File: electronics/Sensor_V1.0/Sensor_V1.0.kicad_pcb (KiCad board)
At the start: 2 copper layers, 45.9 x 25.6 mm, 7 parts, among them J1 nuclone_small_left, J2 nuclone_small_right, J3 PINS_1X18, J4 PINS_1X17

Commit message: WIP schematic definition
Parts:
- added J5: DevBoardUartInput, Connector_JST:JST_PH_S4B-PH-K_1x04_P2.00mm_Horizontal, B.Cu at (84.3, 92.5)
- added R1: 100, SquantorRcl:R_0603_hand, B.Cu at (80.3, 89.2)
- added R2: 100, SquantorRcl:R_0603_hand, B.Cu at (78.3, 89.2)
- added TP1: UART_RX, TestPoint:TestPoint_THTPad_D1.0mm_Drill0.5mm, F.Cu at (80.4, 86.7)
- added TP2: UART_TX, TestPoint:TestPoint_THTPad_D1.0mm_Drill0.5mm, F.Cu at (78.3, 86.7)
- added U1: PPG_sensor, SquantorOpto:PPG_sensor_reverse, F.Cu at (83.9, 80.3)
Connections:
- net /VDD1 renamed /VDD
- net /VDD2 renamed /VDDA
- net /VSS1 renamed /VSS
- net /VSS2 renamed /VSSA
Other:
- outline, holes or cut-outs redrawn

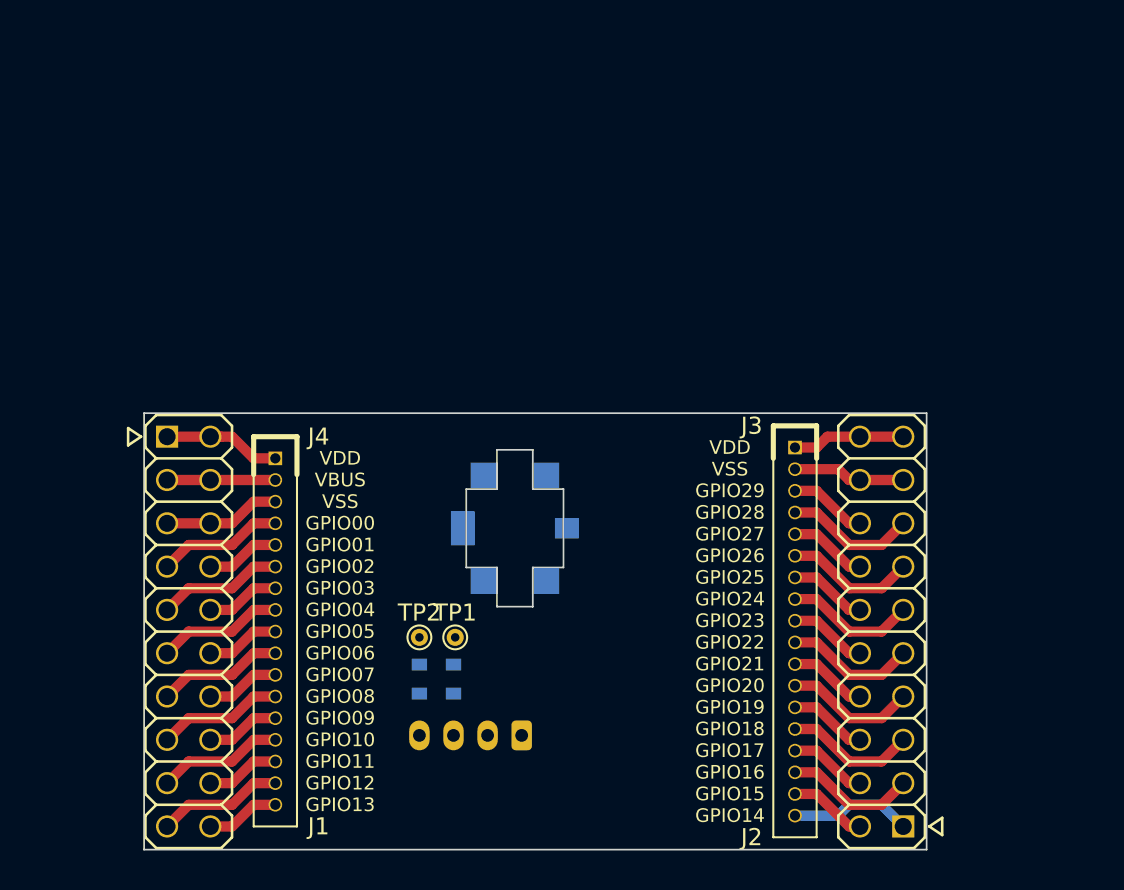
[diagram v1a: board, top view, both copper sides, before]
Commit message: WIP some layout and additional testpoints
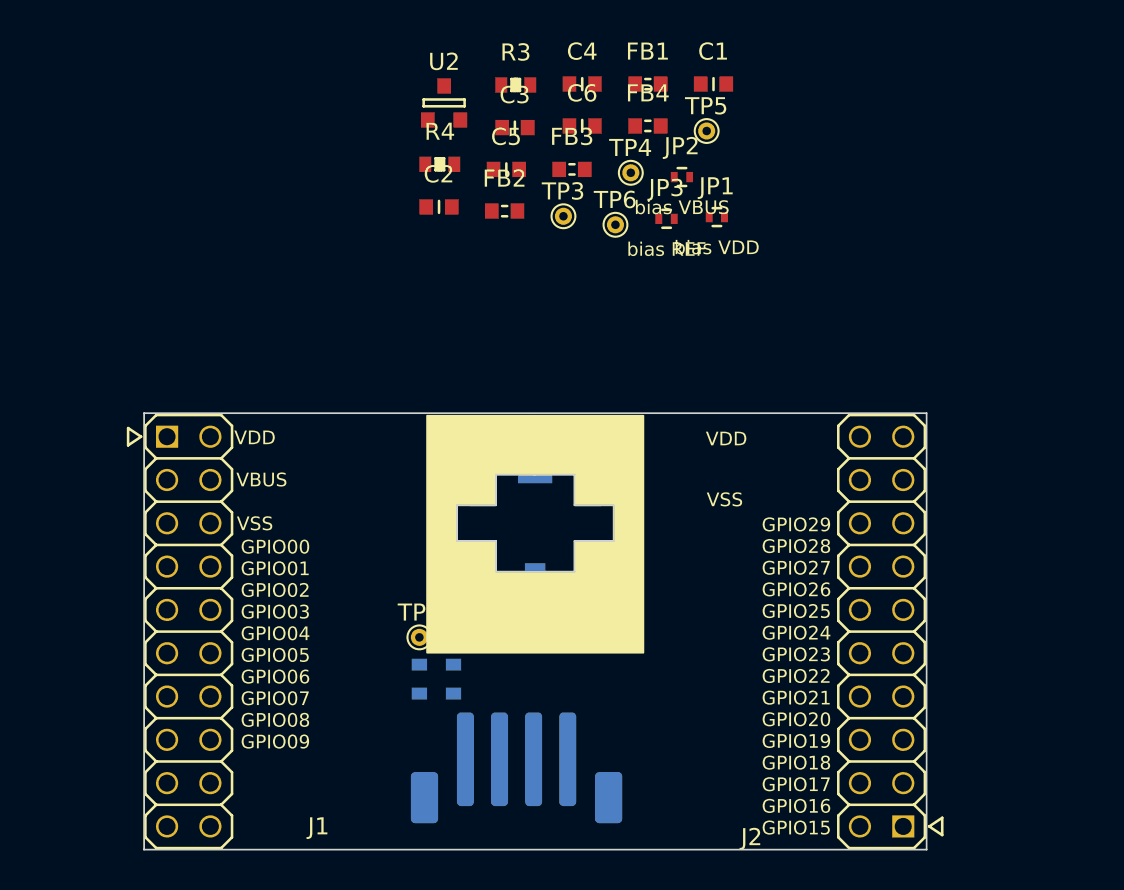
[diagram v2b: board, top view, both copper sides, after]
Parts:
- removed J3: PINS_1X18, SquantorConnectors:Header-0127-1X18-H006
- removed J4: PINS_1X17, SquantorConnectors:Header-0127-1X17-H006
- added C1: 1u, SquantorRcl:C_0603, F.Cu at (95.5, 54.2)
- added C2: 10u, SquantorRcl:C_0603, F.Cu at (79.5, 61.5)
- added C3: 1u, SquantorRcl:C_0603, F.Cu at (83.9, 56.8)
- added C4: 10u, SquantorRcl:C_0603, F.Cu at (87.8, 54.2)
- added C5: 1u, SquantorRcl:C_0603, F.Cu at (83.4, 59.2)
- added C6: 10u, SquantorRcl:C_0603, F.Cu at (87.8, 56.7)
- added FB1: 600, SquantorRcl:L_0603, F.Cu at (91.7, 54.2)
- added FB2: 600, SquantorRcl:L_0603, F.Cu at (83.3, 61.7)
- added FB3: 600, SquantorRcl:L_0603, F.Cu at (87.2, 59.2)
- added FB4: 600, SquantorRcl:L_0603, F.Cu at (91.7, 56.7)
- added JP1: bias VDD, SquantorSpecial:solder_jumper_2way_noconn, F.Cu at (95.8, 62.0)
- added JP2: bias VBUS, SquantorSpecial:solder_jumper_2way_noconn, F.Cu at (93.7, 59.7)
- added JP3: bias REF, SquantorSpecial:solder_jumper_2way_noconn, F.Cu at (92.8, 62.1)
- added R3: 1K, SquantorRcl:R_0603_hand, F.Cu at (84.0, 54.3)
- added R4: 1K, SquantorRcl:R_0603_hand, F.Cu at (79.5, 59.0)
- added TP3: LED1 drive, TestPoint:TestPoint_THTPad_D1.0mm_Drill0.5mm, F.Cu at (86.8, 62.0)
- added TP4: LED2 drive, TestPoint:TestPoint_THTPad_D1.0mm_Drill0.5mm, F.Cu at (90.7, 59.5)
- added TP5: guard, TestPoint:TestPoint_THTPad_D1.0mm_Drill0.5mm, F.Cu at (95.2, 57.0)
- added TP6: guard, TestPoint:TestPoint_THTPad_D1.0mm_Drill0.5mm, F.Cu at (89.8, 62.5)
- added U2: reference_sot23-3, SquantorIC:SOT23-3, F.Cu at (79.8, 55.4)
- J5: footprint Connector_JST:JST_PH_S4B-PH-K_1x04_P2.00mm_Horizontal -> Connector_JST:JST_PH_B4B-PH-SM4-TB_1x04-1MP_P2.00mm_Vertical
- TP1: value UART_RX -> UART RX
- TP2: value UART_TX -> UART TX
- U1: footprint SquantorOpto:PPG_sensor_reverse -> SquantorOpto:PPG_sensor_reverse_PD_antiparallel
- moved J5 1.92 mm to (84.0, 94.3), turned to 0 degrees
- moved U1 1.22 mm to (85.1, 80.0), turned to 270 degrees
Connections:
- net /VDDA renamed /VDDA_RAW
- net /VSSA renamed /VSSA_RAW
- net Net-(U1-Pad5) renamed /PD_OUT
- U1 pad 1: Net-(U1-Pad1) -> /LED1
- U1 pad 2: Net-(U1-Pad2) -> /PD_BIAS
- U1 pad 3: Net-(U1-Pad3) -> /LED2
- U1 pad 4: Net-(U1-Pad4) -> /VSS
- U1 pad 6: Net-(U1-Pad6) -> /VSS
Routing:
- net /GPIO_22: track 7.67 -> 0.00 mm
- net /GPIO_18: track 7.67 -> 0.00 mm
- net /GPIO_28: track 7.67 -> 0.00 mm
- net /GPIO_24: track 7.67 -> 0.00 mm
- net /GPIO_20: track 7.67 -> 0.00 mm
- net /GPIO_16: track 7.67 -> 0.00 mm
- net /GPIO_26: track 7.67 -> 0.00 mm
- net /VDD: track 7.51 -> 0.00 mm
- net /GPIO_12: track 7.40 -> 0.00 mm
- net /GPIO_10: track 7.40 -> 0.00 mm
- net /GPIO_06: track 7.40 -> 0.00 mm
- net /GPIO_02: track 7.40 -> 0.00 mm
- net /GPIO_08: track 7.40 -> 0.00 mm
- net /GPIO_04: track 7.40 -> 0.00 mm
- net /GPIO_00: track 7.40 -> 0.00 mm
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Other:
- outline, holes or cut-outs redrawn
- board text removed: "GPIO10"
- board text removed: "GPIO11"
- board text removed: "GPIO12"
- board text removed: "GPIO13"
- board text removed: "GPIO14"

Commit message: WIP more layout and extra testpoints added, next step are my own testpoints, those from kicad are just annoying
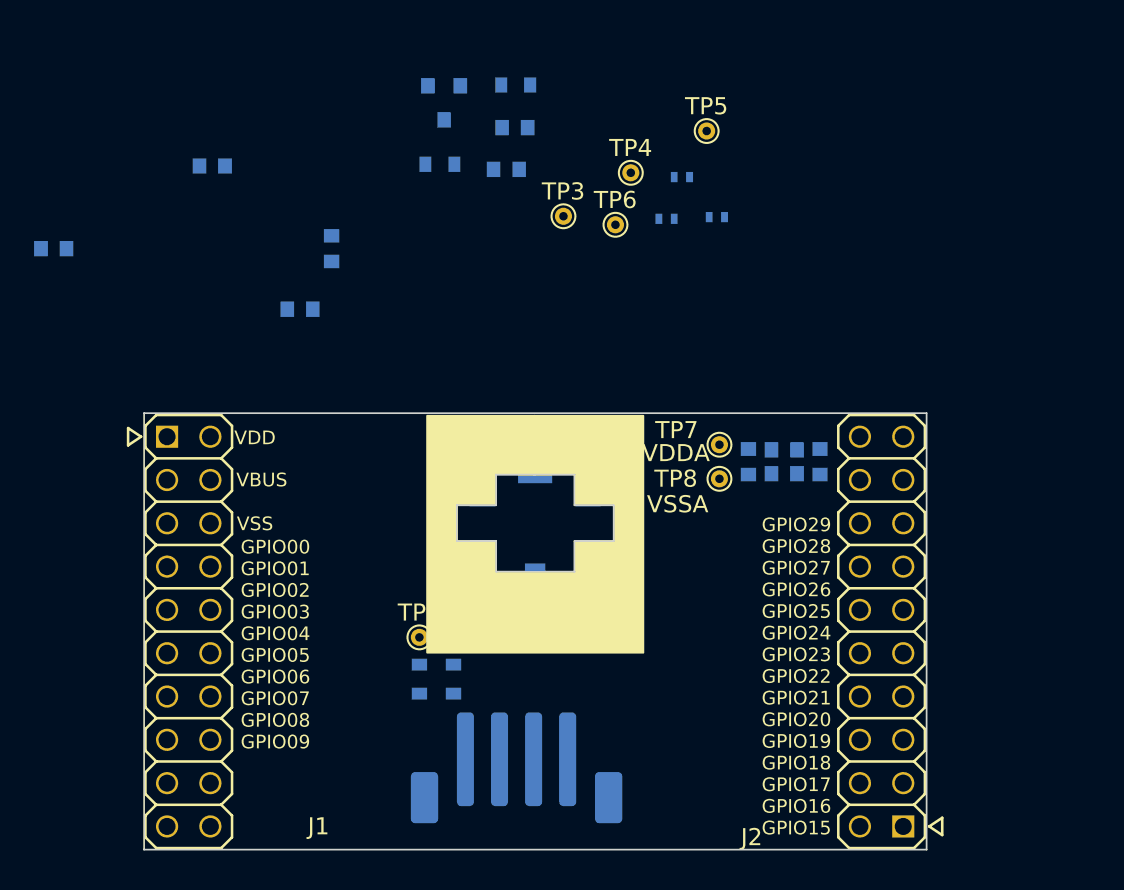
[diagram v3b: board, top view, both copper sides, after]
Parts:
- added TP7: VDDA, TestPoint:TestPoint_THTPad_D1.0mm_Drill0.5mm, F.Cu at (95.9, 75.4)
- added TP8: VSSA, TestPoint:TestPoint_THTPad_D1.0mm_Drill0.5mm, F.Cu at (95.9, 77.4)
- C1, C2, C3, C4, C5, C6, FB1, FB2, FB3, FB4, JP1, JP2, JP3, R3, R4, U2: moved to B.Cu
- moved FB3 30.8 mm to (56.9, 63.9)
- moved FB4 25.7 mm to (66.2, 59.0), turned to 180 degrees
- moved C2 23.5 mm to (97.6, 76.4), turned to 270 degrees
- moved C1 23.0 mm to (101.8, 76.4), turned to 270 degrees
- moved FB1 22.9 mm to (99.7, 75.7)
- moved FB2 22.5 mm to (99.7, 77.1)
- moved C4 21.2 mm to (71.3, 67.5)
- moved C6 16.4 mm to (73.2, 63.9), turned to 270 degrees

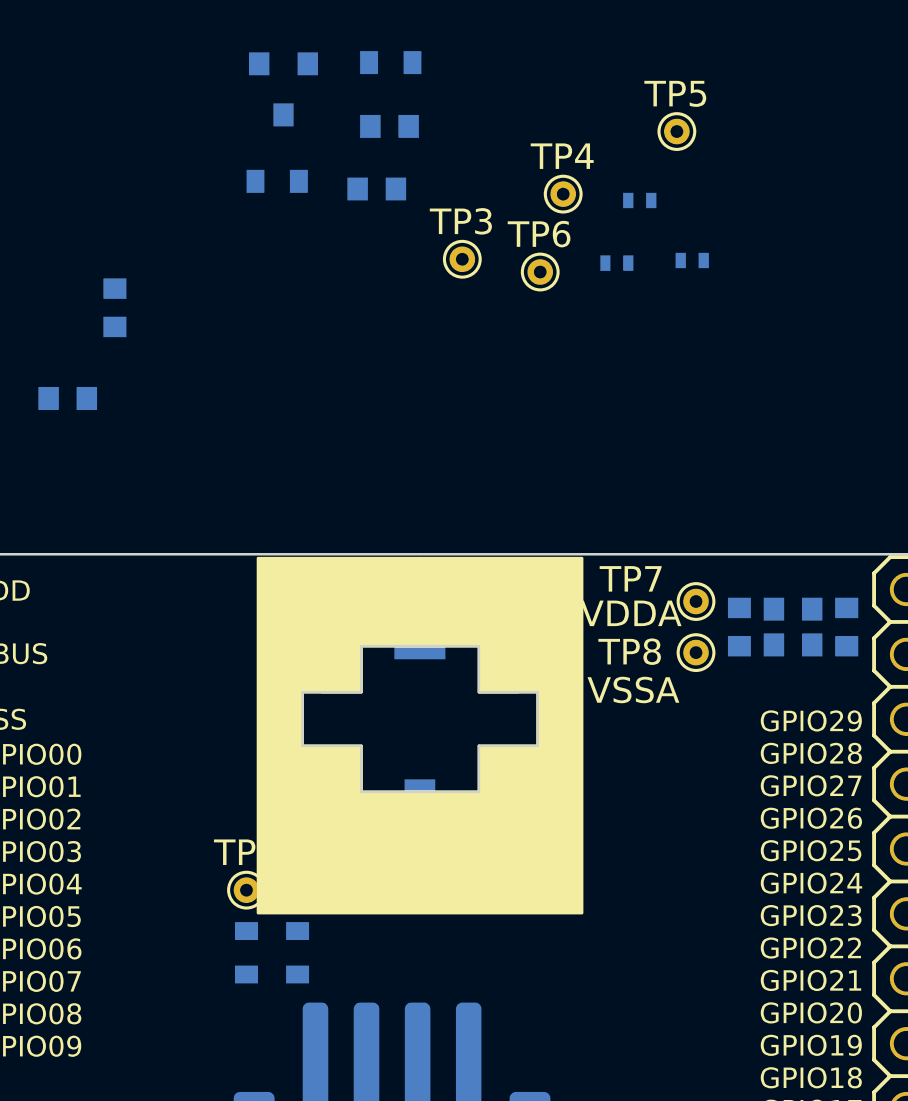
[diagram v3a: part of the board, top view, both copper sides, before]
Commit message: updated testpoints to something smaller
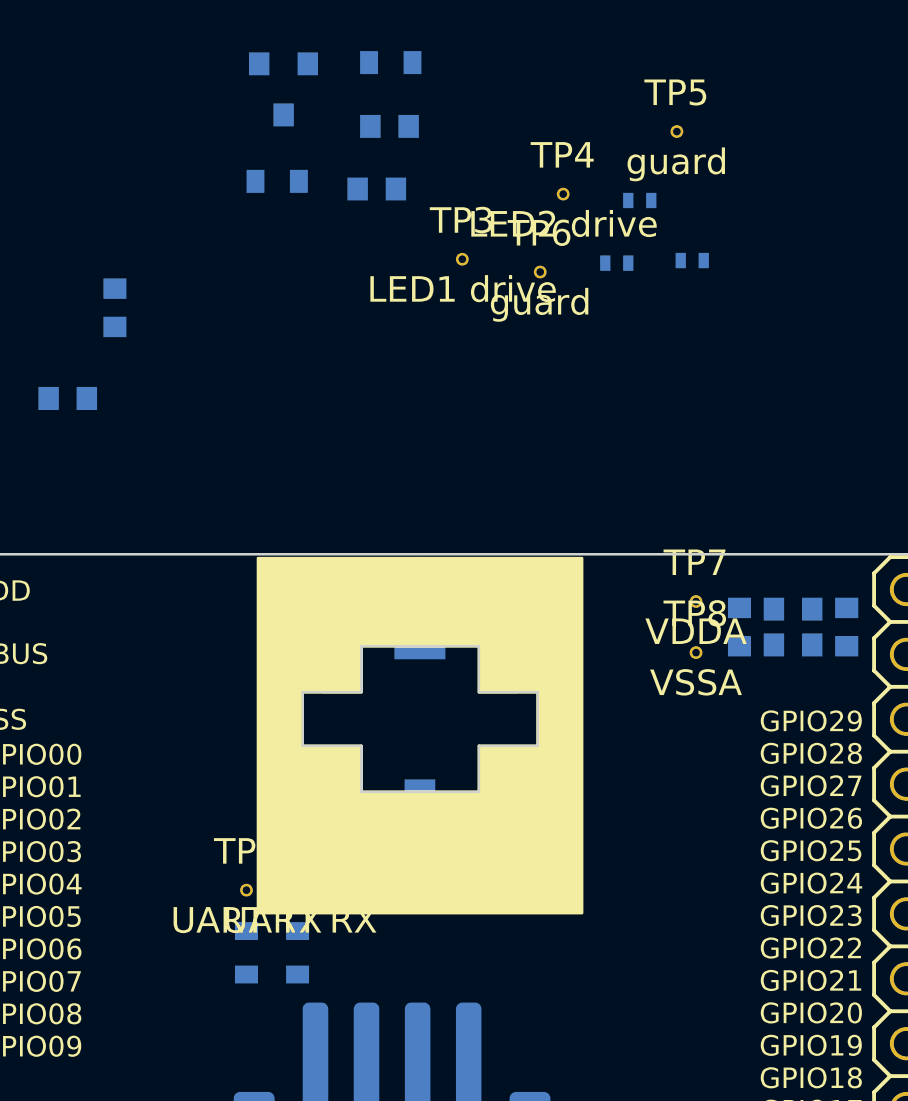
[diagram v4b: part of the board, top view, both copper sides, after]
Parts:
- TP1, TP2, TP3, TP4, TP5, TP6, TP7, TP8: footprint TestPoint:TestPoint_THTPad_D1.0mm_Drill0.5mm -> SquantorTestPoints:TestPoint_hole_H03R05

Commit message: WIP some placement and component changes
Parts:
- TP1: value UART RX -> RX
- TP2: value UART TX -> TX
- TP3: value LED1 drive -> LED1
- TP4: value LED2 drive -> LED2
- moved R3 24.0 mm to (74.5, 76.4), turned to 180 degrees
- moved TP4 23.8 mm to (72.6, 74.9)
- moved TP6 21.8 mm to (83.8, 83.5)
- moved TP3 20.2 mm to (72.6, 76.4)
- moved R4 16.7 mm to (74.5, 74.9), turned to 180 degrees
- moved TP1 7.97 mm to (73.1, 89.9)
- moved TP2 5.47 mm to (73.1, 88.4)
- moved R1 5.35 mm to (75.0, 89.9), turned to 0 degrees
- moved J5 5.00 mm to (79.0, 94.4)
- moved R2 3.38 mm to (75.0, 88.4), turned to 0 degrees
- moved TP7 0.67 mm to (96.5, 75.1)
- moved TP8 0.60 mm to (96.5, 77.4)
- moved C1 0.22 mm to (101.9, 76.2)
- moved C2 0.22 mm to (97.7, 76.2)
- moved FB1 0.22 mm to (99.8, 75.5)
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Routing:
- net /VSSA_RAW: track 0.00 -> 6.37 mm
- net /VDDA_RAW: track 0.00 -> 6.37 mm
- net /VSSA: track 0.00 -> 2.76 mm
- net /VDDA: track 0.00 -> 2.72 mm
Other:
- board text added: "P02"
- board text added: "P03"
- board text added: "P04"
- board text added: "P05"
- board text added: "P10"
- board text added: "P11"
- board text added: "P12"
- board text added: "P13"
- board text added: "P16"
- board text added: "P17"
- board text removed: "GPIO00"
- board text removed: "GPIO01"
- board text removed: "GPIO02"
- board text removed: "GPIO03"
- board text removed: "GPIO04"
- board text removed: "GPIO05"
- board text removed: "GPIO06"
- board text removed: "GPIO07"
- board text removed: "GPIO08"
- board text removed: "GPIO09"
